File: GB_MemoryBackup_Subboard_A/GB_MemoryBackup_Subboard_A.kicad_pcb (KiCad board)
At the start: 2 copper layers, 55.5 x 35 mm, 4 parts, among them J1 Conn_02x16_Odd_Even, J2 GB_Cart_Slot-1Row-32Pins

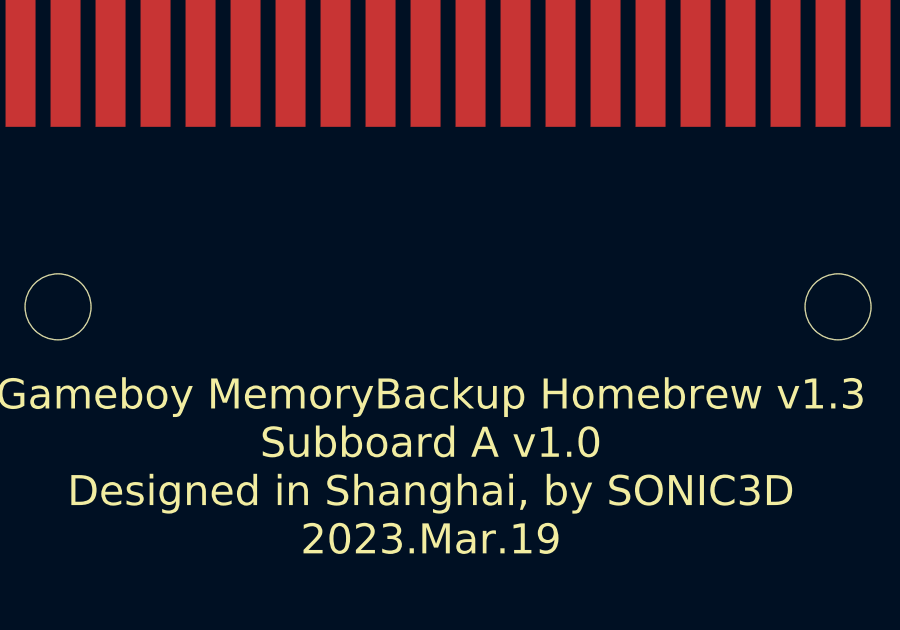
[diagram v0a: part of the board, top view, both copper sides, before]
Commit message: Modified: Added JLCPCB batch string placement.
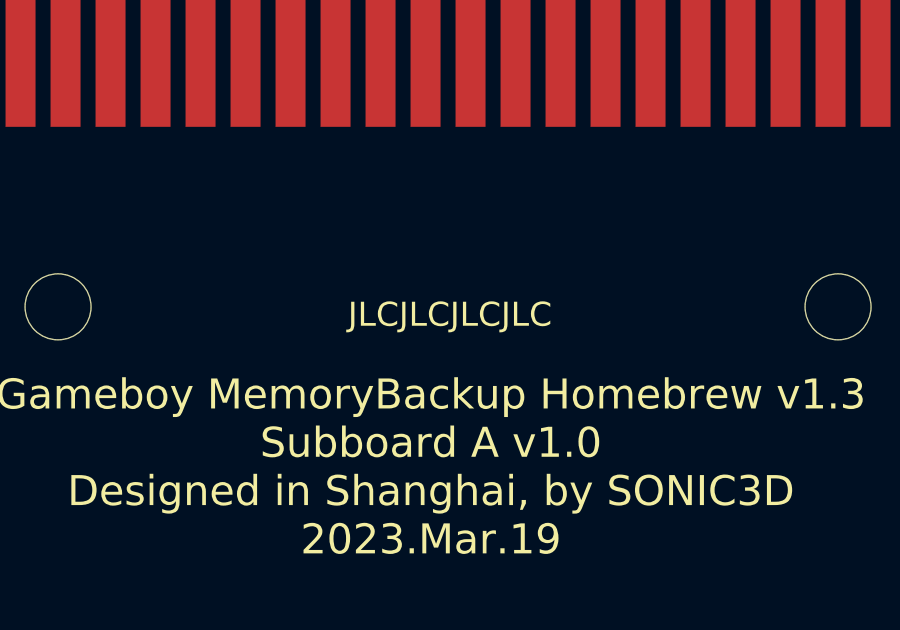
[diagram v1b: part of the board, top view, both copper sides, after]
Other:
- board text added: "JLCJLCJLCJLC"

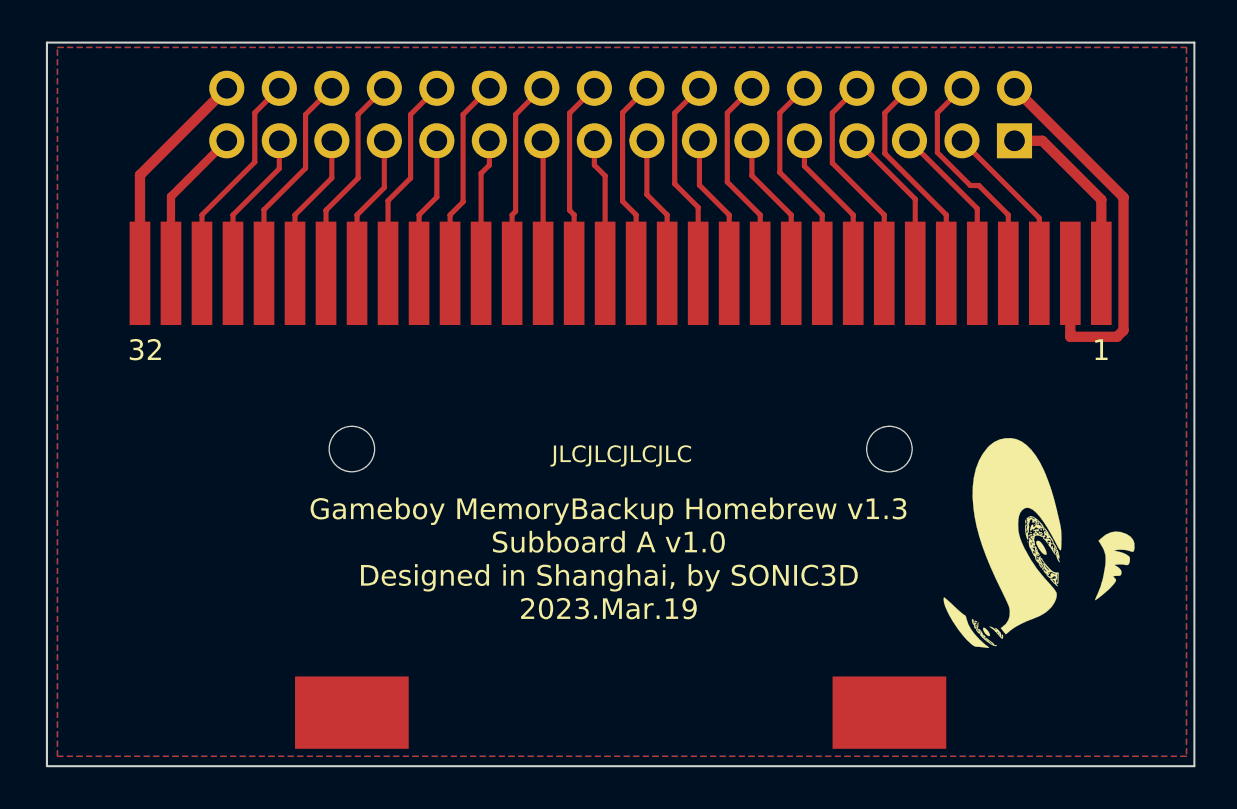
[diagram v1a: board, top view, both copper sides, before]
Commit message: Modified: SubBoard v1.1. Added diode, diode skipping solderjumper, and power indication led.
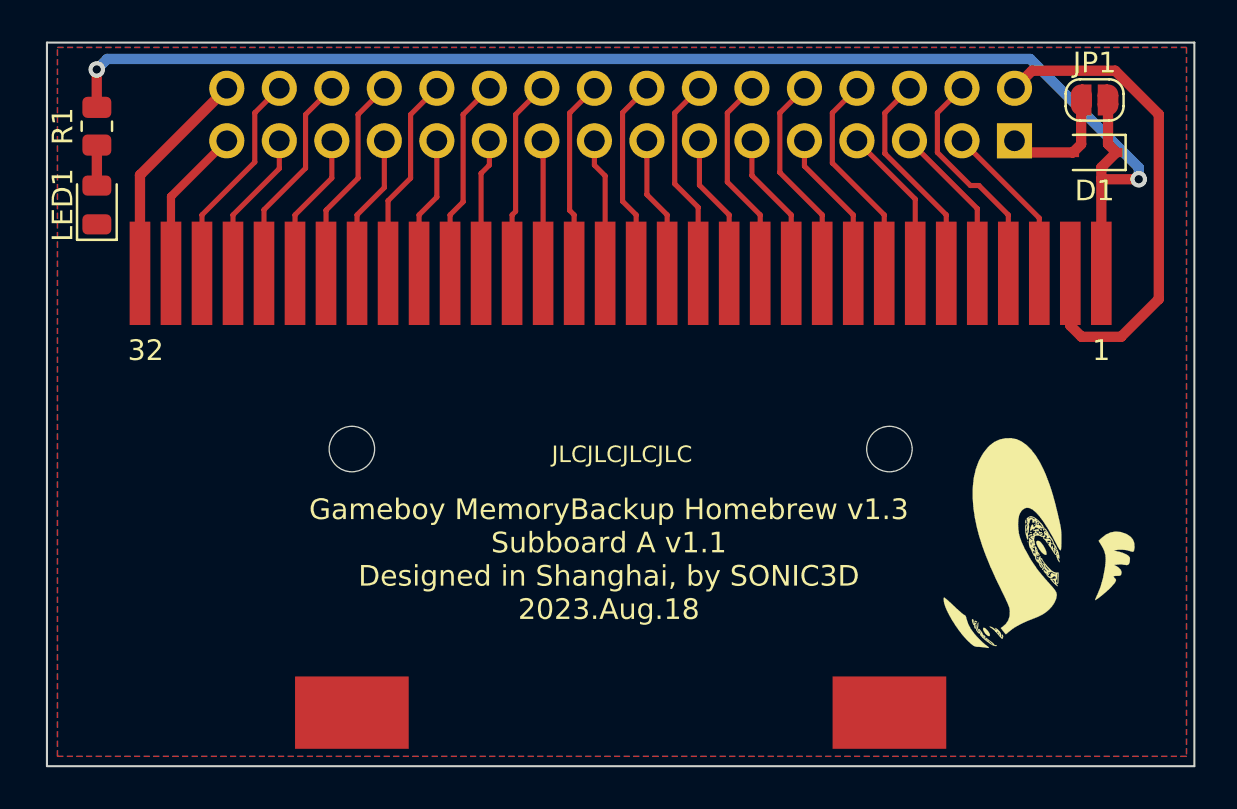
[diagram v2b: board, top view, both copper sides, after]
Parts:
- added D1: 1N4148WS, Diode_SMD:D_SOD-323, F.Cu at (192.4, 87.0)
- added JP1: SJ_SkipDiode, Jumper:SolderJumper-2_P1.3mm_Open_RoundedPad1.0x1.5mm, F.Cu at (192.4, 84.5)
- added LED1: PowerLED_Red, Diode_SMD:D_0805_2012Metric, F.Cu at (144.1, 89.5)
- added R1: 10K, Resistor_SMD:R_0805_2012Metric, F.Cu at (144.1, 85.7)
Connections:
- J2 pad 1: +5V -> /CartSlot_5V_Input
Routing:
- net /CartSlot_5V_Input: track 0.00 -> 65.8 mm, vias 0 -> 2
- net /ACLK: track 19.7 -> 24.9 mm
- net +5V: track 8.94 -> 5.76 mm
- net /PwrLED_5V_Input: track 0.00 -> 1.96 mm
- added copper zone on B.Cu, net /CartSlot_5V_Input
- removed copper zone on B.Cu, net +5V
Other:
- board text added: "Gameboy MemoryBackup Homebrew v1.3 Subboard A v1.1 Designed in Shanghai, by SONIC3D 2023.Aug.18"
- board text added: "Gameboy MemoryBackup Homebrew v1.3 Subboard A v1.1 https://github.com/SONIC3D/gameboy-memorybackup Designed in Shanghai, by SONIC3D 2023.Aug.18"
- board text removed: "Gameboy MemoryBackup Homebrew v1.3 Subboard A v1.0 Designed in Shanghai, by SONIC3D 2023.Mar.19"
- board text removed: "Gameboy MemoryBackup Homebrew v1.3 Subboard A v1.0 https://github.com/SONIC3D/gameboy-memorybackup Designed in Shanghai, by SONIC3D 2023.Mar.19"
